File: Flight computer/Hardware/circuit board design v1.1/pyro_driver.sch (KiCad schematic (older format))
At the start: 8 parts, among them J3 Screw_Terminal_01x04, U6 Si7232DN

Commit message: put in new acclerometers and 9dof sensor. Changed supplier from mouser to farnell and RS
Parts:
- U6: min_quantity (none) -> 20
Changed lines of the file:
@@
 F 4 "https://uk.rs-online.com/web/p/mosfets/8181396/" H 5850 2600 50  0001 C CNN "Purchase link"
 F 5 "0.729" H 5850 2600 50  0001 C CNN "Cost"
+F 6 "20" H 5850 2600 50  0001 C CNN "min_quantity"
 	2    5850 2600
 	1    0    0    -1
@@
 F 4 "https://uk.rs-online.com/web/p/mosfets/8181396/" H 5850 1350 50  0001 C CNN "Purchase link"
 F 5 "0.729" H 5850 1350 50  0001 C CNN "Cost"
+F 6 "20" H 5850 1350 50  0001 C CNN "min_quantity"
 	1    5850 1350
 	1    0    0    -1

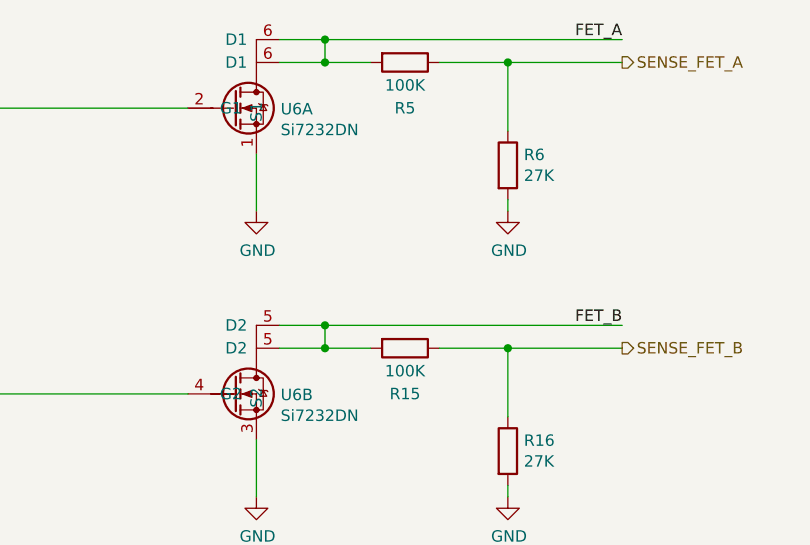
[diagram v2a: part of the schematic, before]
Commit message: put in logo for V1.1
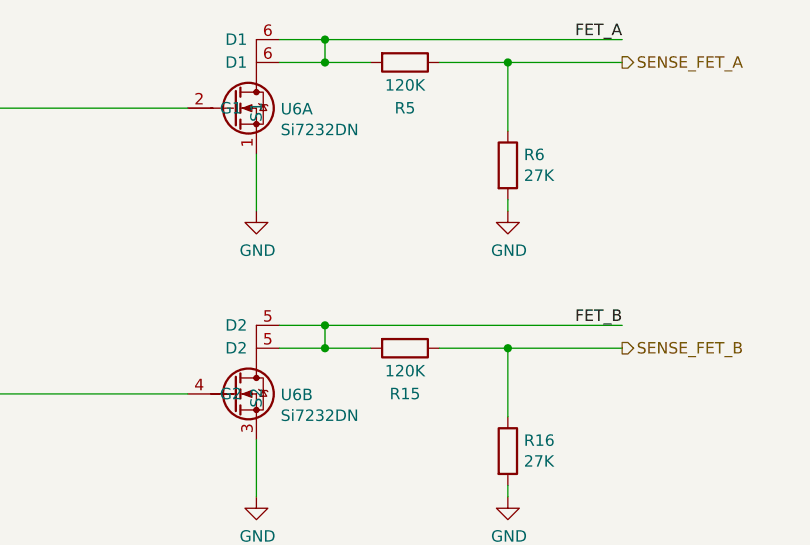
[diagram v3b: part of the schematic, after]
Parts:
- R15, R5: value 100K -> 120K; Cost (none) -> 0.035; Purchase link (none) -> https://uk.rs-online.com/web/p/surface-mount-fixed-resistor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; min_quantity (none) -> 50
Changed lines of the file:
@@
 P 6500 2850
 F 0 "R15" V 6700 2850 50  0000 C CNN
-F 1 "100K" V 6600 2850 50  0000 C CNN
+F 1 "120K" V 6600 2850 50  0000 C CNN
 F 2 "Resistor_SMD:R_0603_1608Metric" V 6430 2850 50  0001 C CNN
 F 3 "~" H 6500 2850 50  0001 C CNN
+F 4 "0.035" H 6500 2850 50  0001 C CNN "Cost"
+F 5 "https://uk.rs-online.com/web/p/surface-mount-fixed-resistors/6789715/" H 6500 2850 50  0001 C CNN "Purchase link"
+F 6 "50" H 6500 2850 50  0001 C CNN "min_quantity"
 	1    6500 2850
 	0    1    1    0
@@
 P 6500 1600
 F 0 "R5" V 6700 1600 50  0000 C CNN
-F 1 "100K" V 6600 1600 50  0000 C CNN
+F 1 "120K" V 6600 1600 50  0000 C CNN
 F 2 "Resistor_SMD:R_0603_1608Metric" V 6430 1600 50  0001 C CNN
 F 3 "~" H 6500 1600 50  0001 C CNN
+F 4 "0.035" H 6500 1600 50  0001 C CNN "Cost"
+F 5 "https://uk.rs-online.com/web/p/surface-mount-fixed-resistors/6789715/" H 6500 1600 50  0001 C CNN "Purchase link"
+F 6 "50" H 6500 1600 50  0001 C CNN "min_quantity"
 	1    6500 1600
 	0    1    1    0

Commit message: changed GPS to M8Q and included the diode from V bus to foot print which I missed out
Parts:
- R13, R3: Cost (none) -> 0.002; Purchase link (none) -> https://uk.rs-online.com/web/p/surface-mount-fixed-resistor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; min_quantity (none) -> 10
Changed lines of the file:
@@
 F 2 "Resistor_SMD:R_0603_1608Metric" V 4380 3350 50  0001 C CNN
 F 3 "~" H 4450 3350 50  0001 C CNN
+F 4 "0.002" H 4450 3350 50  0001 C CNN "Cost"
+F 5 "https://uk.rs-online.com/web/p/surface-mount-fixed-resistors/8306410/" H 4450 3350 50  0001 C CNN "Purchase link"
+F 6 "10" H 4450 3350 50  0001 C CNN "min_quantity"
 	1    4450 3350
 	1    0    0    -1
@@
 F 2 "Resistor_SMD:R_0603_1608Metric" V 4380 2100 50  0001 C CNN
 F 3 "~" H 4450 2100 50  0001 C CNN
+F 4 "0.002" H 4450 2100 50  0001 C CNN "Cost"
+F 5 "https://uk.rs-online.com/web/p/surface-mount-fixed-resistors/8306410/" H 4450 2100 50  0001 C CNN "Purchase link"
+F 6 "10" H 4450 2100 50  0001 C CNN "min_quantity"
 	1    4450 2100
 	1    0    0    -1

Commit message: put in the last bom purchase links
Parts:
- R16, R6: value 27K -> 22K; Cost (none) -> 0.028; Purchase link (none) -> https://uk.rs-online.com/web/p/surface-mount-fixed-resistor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; min_quantity (none) -> 50
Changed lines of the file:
@@
 P 6950 3300
 F 0 "R16" H 7020 3346 50  0000 L CNN
-F 1 "27K" H 7020 3255 50  0000 L CNN
+F 1 "22K" H 7020 3255 50  0000 L CNN
 F 2 "Resistor_SMD:R_0603_1608Metric" V 6880 3300 50  0001 C CNN
 F 3 "~" H 6950 3300 50  0001 C CNN
+F 4 "0.028" H 6950 3300 50  0001 C CNN "Cost"
+F 5 "https://uk.rs-online.com/web/p/surface-mount-fixed-resistors/7408855/" H 6950 3300 50  0001 C CNN "Purchase link"
+F 6 "50" H 6950 3300 50  0001 C CNN "min_quantity"
 	1    6950 3300
 	1    0    0    -1
@@
 P 6950 2050
 F 0 "R6" H 7020 2096 50  0000 L CNN
-F 1 "27K" H 7020 2005 50  0000 L CNN
+F 1 "22K" H 7020 2005 50  0000 L CNN
 F 2 "Resistor_SMD:R_0603_1608Metric" V 6880 2050 50  0001 C CNN
 F 3 "~" H 6950 2050 50  0001 C CNN
+F 4 "0.028" H 6950 2050 50  0001 C CNN "Cost"
+F 5 "https://uk.rs-online.com/web/p/surface-mount-fixed-resistors/7408855/" H 6950 2050 50  0001 C CNN "Purchase link"
+F 6 "50" H 6950 2050 50  0001 C CNN "min_quantity"
 	1    6950 2050
 	1    0    0    -1
